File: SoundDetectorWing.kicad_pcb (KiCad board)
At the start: 2 copper layers, 50.8 x 22.9 mm, 17 parts, among them J1 feather long, J2 feather short, J3 sound detector

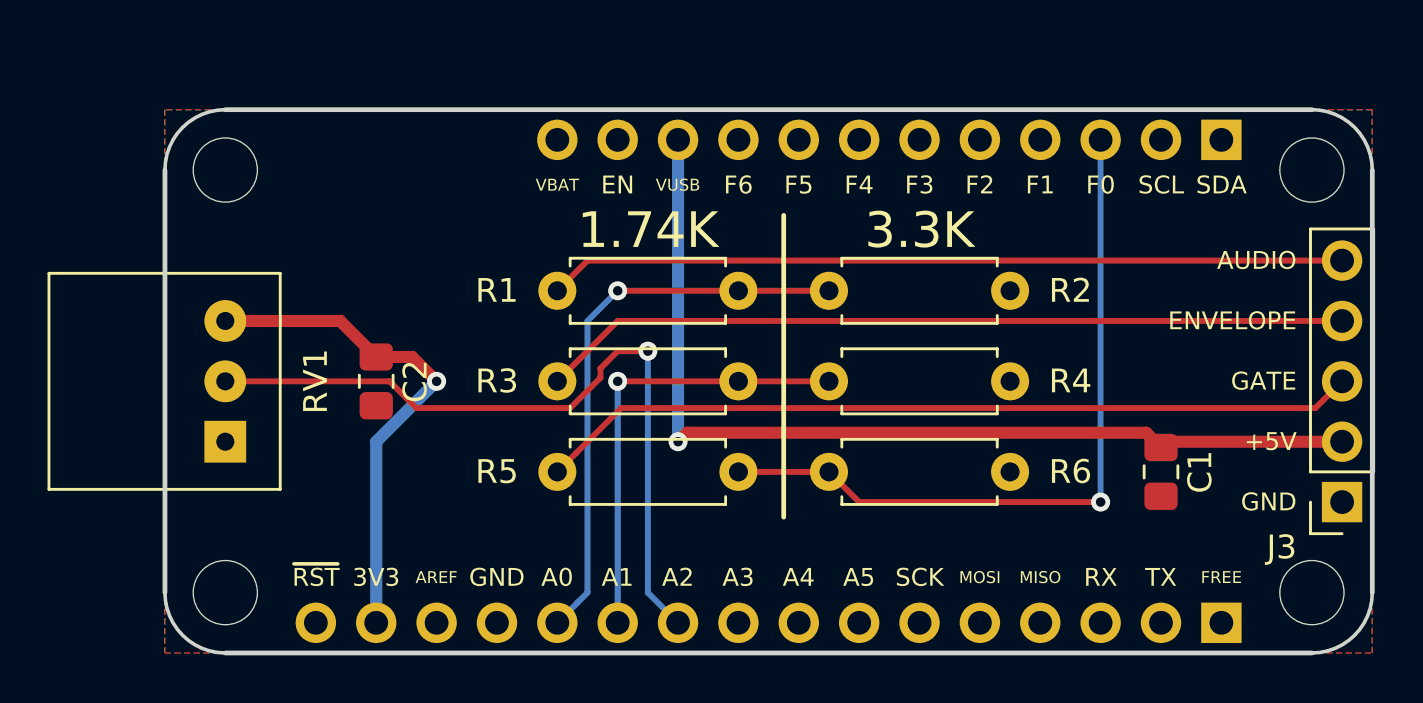
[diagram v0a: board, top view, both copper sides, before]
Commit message: Add screw holes to line up with SparkFun Sound Detector board.
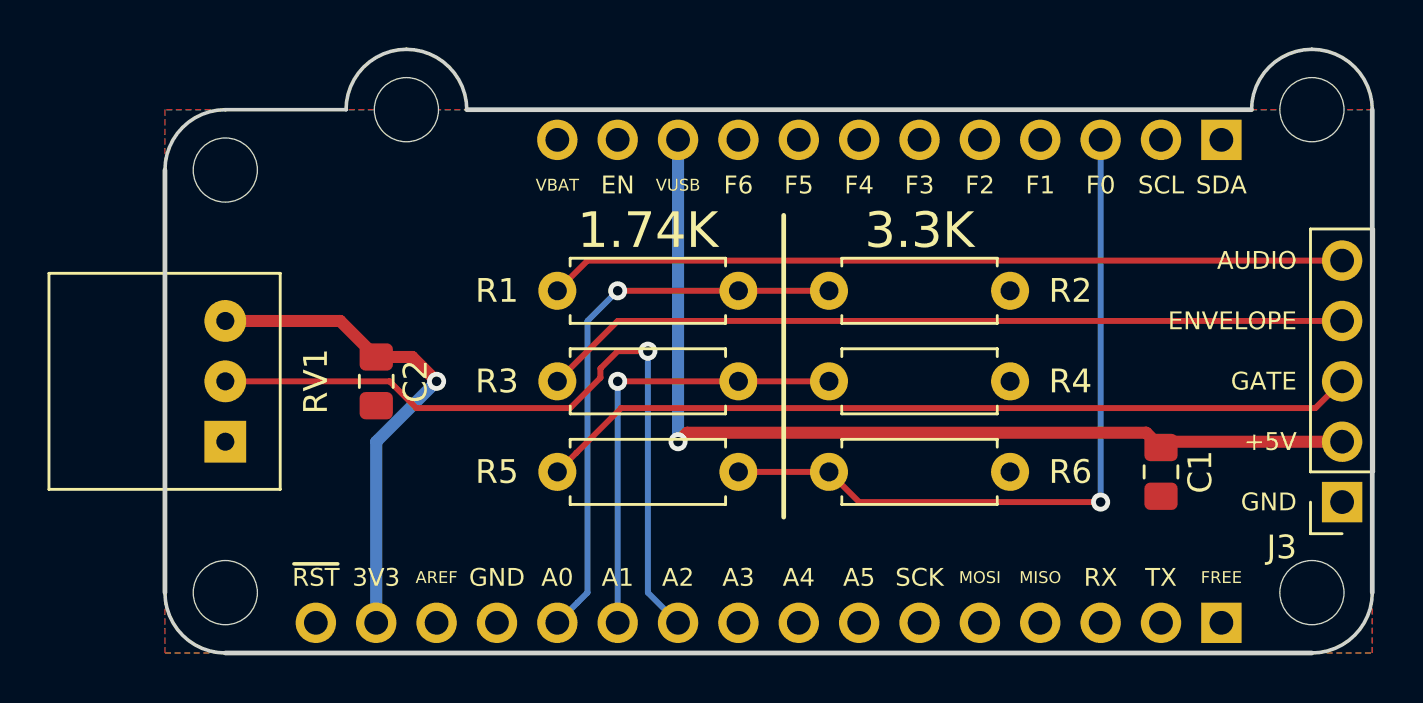
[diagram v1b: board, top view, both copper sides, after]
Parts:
- added REF**: MountingHole_2.7mm_M2.5, MountingHole:MountingHole_2.7mm_M2.5, F.Cu at (35.6, 25.4)
- moved REF** 2.54 mm to (73.7, 25.4)
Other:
- board size 50.8 x 22.9 mm -> 50.8 x 25.4 mm
- board text added: "2019-08-09"
- board text added: "Sound Detector FeatherWing 1.0.1"
- board text removed: "2019-07-24"
- board text removed: "Sound Detector FeatherWing 1.0"
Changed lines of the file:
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@@
   (general
     (thickness 1.6)
-    (drawings 49)
+    (drawings 53)
     (tracks 48)
     (zones 0)
-    (modules 17)
+    (modules 18)
     (nets 32)
   )
@@
   (title_block
     (title "Sound Detector FeatherWing")
-    (date 2019-07-24)
-    (rev 1.0)
+    (date 2019-08-09)
+    (rev 1.0.1)
     (company "Patrick Pelletier")
   )
@@
   )
   (module MountingHole:MountingHole_2.7mm_M2.5 locked (layer F.Cu)
-    (at 73.66 27.94)
+    (at 35.56 25.4)
+    (descr "Mounting Hole 2.7mm, no annular, M2.5")
+    (tags "mounting hole 2.7mm no annular m2.5")
+    (attr virtual)
+    (fp_text reference REF** (at 0 -3.7) (layer F.SilkS) hide
+      (effects (font (size 1 1) (thickness 0.15)))
+    )
+    (fp_text value MountingHole_2.7mm_M2.5 (at 0 3.7) (layer F.Fab) hide
+      (effects (font (size 1 1) (thickness 0.15)))
+    )
+    (fp_circle (center 0 0) (end 2.95 0) (layer F.CrtYd) (width 0.05))
+    (fp_circle (center 0 0) (end 2.7 0) (layer Cmts.User) (width 0.15))
+    (fp_text user %R (at 0.3 0) (layer F.Fab) hide
+      (effects (font (size 1 1) (thickness 0.15)))
+    )
+    (pad 1 np_thru_hole circle (at 0 0) (size 2.7 2.7) (drill 2.7) (layers *.Cu *.Mask))
+  )
+  (module MountingHole:MountingHole_2.7mm_M2.5 locked (layer F.Cu)
+    (at 73.66 25.4)
     (descr "Mounting Hole 2.7mm, no annular, M2.5")
     (tags "mounting hole 2.7mm no annular m2.5")
@@
       (xy 0.555814 2.531069)) (layer B.SilkS) (width 0.01))
   )
+  (gr_line (start 33.02 25.4) (end 27.94 25.4) (layer Edge.Cuts) (width 0.15))
+  (gr_arc (start 35.56 25.4) (end 35.56 22.86) (angle -90) (layer Edge.Cuts) (width 0.15))
+  (gr_arc (start 35.56 25.4) (end 38.1 25.4) (angle -90) (layer Edge.Cuts) (width 0.15))
+  (gr_arc (start 73.66 25.4) (end 73.66 22.86) (angle -90) (layer Edge.Cuts) (width 0.15))
   (gr_text https://github.com/ppelleti/SoundDetectorWing (at 51.435 34.925) (layer B.SilkS)
     (effects (font (size 0.75 0.75) (thickness 0.15)) (justify mirror))
@@
     (effects (font (size 1 1) (thickness 0.2)) (justify mirror))
   )
-  (gr_text 2019-07-24 (at 31.75 36.83 90) (layer B.SilkS)
+  (gr_text 2019-08-09 (at 31.75 36.83 90) (layer B.SilkS)
     (effects (font (size 1.5 1.5) (thickness 0.3)) (justify mirror))
   )
@@
     (effects (font (size 1.5 1.5) (thickness 0.3)) (justify mirror))
   )
-  (gr_text "Sound Detector FeatherWing 1.0" (at 53.34 30.48) (layer B.SilkS)
+  (gr_text "Sound Detector FeatherWing 1.0.1" (at 53.34 30.48) (layer B.SilkS)
     (effects (font (size 1.5 1.5) (thickness 0.3)) (justify mirror))
   )
@@
     (effects (font (size 0.75 0.75) (thickness 0.15)))
   )
-  (gr_arc (start 73.66 27.94) (end 76.2 27.94) (angle -90) (layer Edge.Cuts) (width 0.15))
+  (gr_arc (start 73.66 25.4) (end 76.2 25.4) (angle -90) (layer Edge.Cuts) (width 0.15))
   (gr_arc (start 73.66 45.72) (end 73.66 48.26) (angle -90) (layer Edge.Cuts) (width 0.15))
   (gr_arc (start 27.94 45.72) (end 25.4 45.72) (angle -90) (layer Edge.Cuts) (width 0.15))
@@
   (gr_line (start 25.4 45.72) (end 25.4 27.94) (layer Edge.Cuts) (width 0.2))
   (gr_line (start 73.66 48.26) (end 27.94 48.26) (layer Edge.Cuts) (width 0.2))
-  (gr_line (start 76.2 27.94) (end 76.2 45.72) (layer Edge.Cuts) (width 0.2))
-  (gr_line (start 27.94 25.4) (end 73.66 25.4) (layer Edge.Cuts) (width 0.2))
+  (gr_line (start 76.2 25.4) (end 76.2 45.72) (layer Edge.Cuts) (width 0.2))
+  (gr_line (start 38.1 25.4) (end 71.12 25.4) (layer Edge.Cuts) (width 0.2))
   (segment (start 43.724999 36.680003) (end 43.724999 36.285001) (width 0.25) (layer F.Cu) (net 10))
   (segment (start 27.94 36.83) (end 34.85319 36.83) (width 0.25) (layer F.Cu) (net 10))

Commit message: Label the functions of the feather pins.
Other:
- board text added: "ENV"
- board text added: "POT"
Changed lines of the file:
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@@
   (general
     (thickness 1.6)
-    (drawings 53)
+    (drawings 57)
     (tracks 48)
     (zones 0)
@@
       (xy 0.555814 2.531069)) (layer B.SilkS) (width 0.01))
   )
+  (gr_text POT (at 46.99 44.45 90) (layer F.SilkS)
+    (effects (font (size 0.75 0.75) (thickness 0.15)) (justify left))
+  )
+  (gr_text ENV (at 44.45 44.45 90) (layer F.SilkS)
+    (effects (font (size 0.75 0.75) (thickness 0.15)) (justify left))
+  )
+  (gr_text AUDIO (at 41.91 44.45 90) (layer F.SilkS)
+    (effects (font (size 0.5 0.5) (thickness 0.1)) (justify left))
+  )
+  (gr_text GATE (at 64.77 29.21 90) (layer F.SilkS)
+    (effects (font (size 0.75 0.75) (thickness 0.15)) (justify right))
+  )
   (gr_line (start 33.02 25.4) (end 27.94 25.4) (layer Edge.Cuts) (width 0.15))

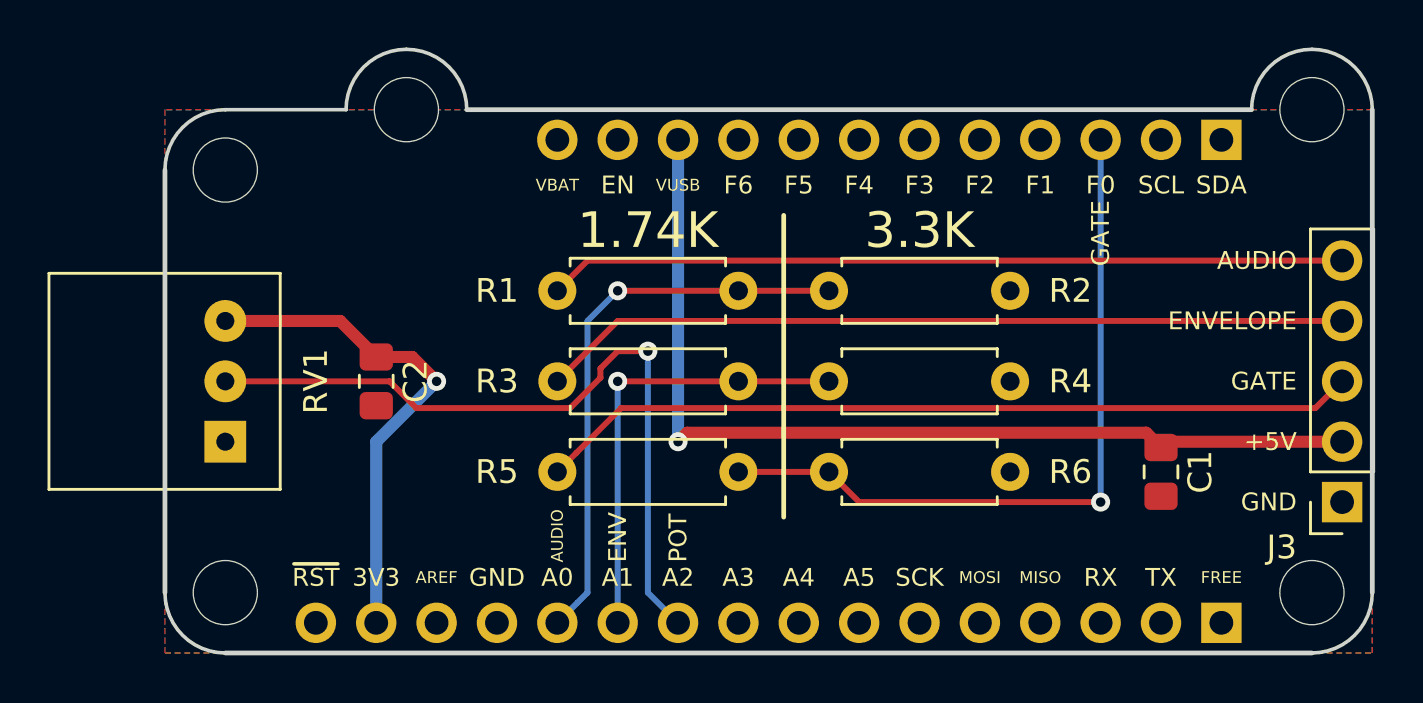
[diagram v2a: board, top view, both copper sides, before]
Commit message: Finally get SoundDetector mounting holes in correct place.
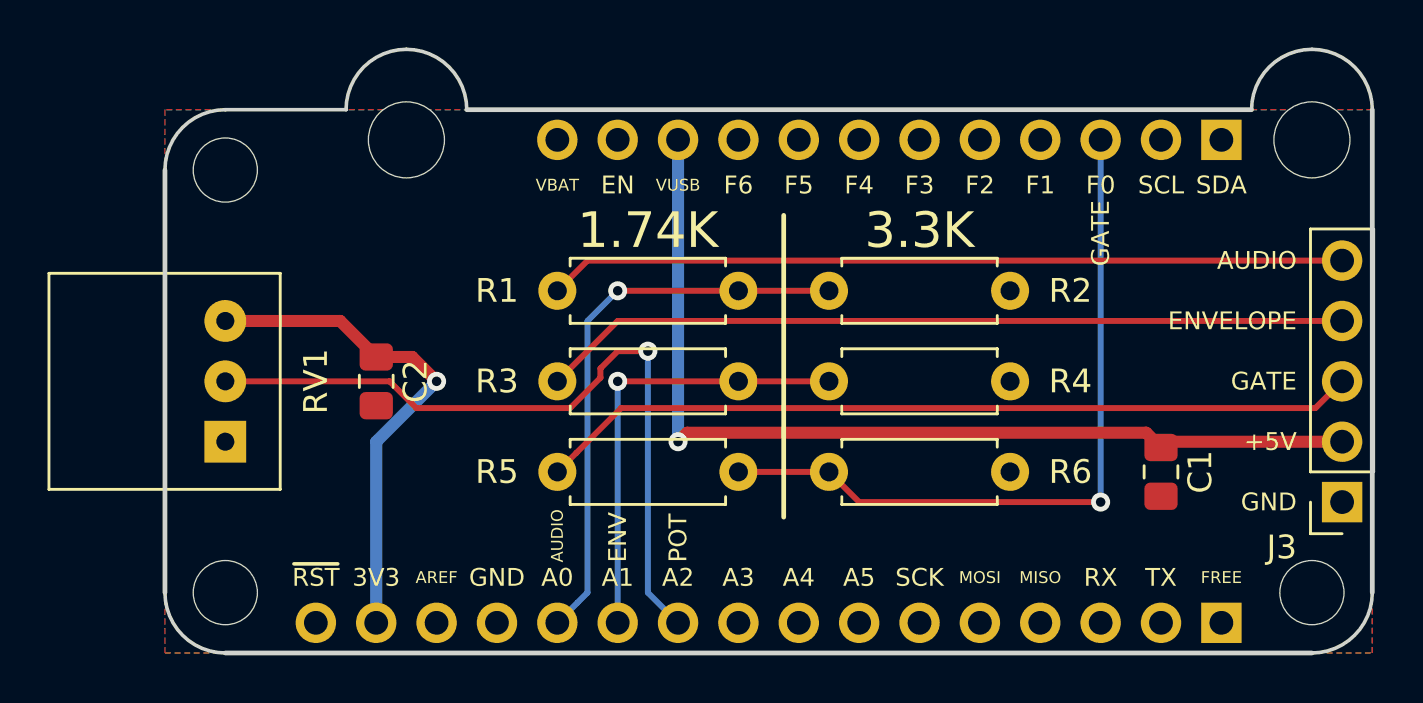
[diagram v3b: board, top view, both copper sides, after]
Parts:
- removed the REF** at (35.6, 25.4)
- removed the REF** at (73.7, 25.4)
- added REF**: MountingHole_3.2mm_M3, MountingHole:MountingHole_3.2mm_M3, F.Cu at (73.7, 26.7)
- added REF**: MountingHole_3.2mm_M3, MountingHole:MountingHole_3.2mm_M3, F.Cu at (35.6, 26.7)
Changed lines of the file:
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@@
     (add_net GND)
   )
-  (module MountingHole:MountingHole_2.7mm_M2.5 locked (layer F.Cu)
-    (at 35.56 25.4)
-    (descr "Mounting Hole 2.7mm, no annular, M2.5")
-    (tags "mounting hole 2.7mm no annular m2.5")
+  (module MountingHole:MountingHole_3.2mm_M3 (layer F.Cu)
+    (at 73.66 26.67)
+    (descr "Mounting Hole 3.2mm, no annular, M3")
+    (tags "mounting hole 3.2mm no annular m3")
     (attr virtual)
-    (fp_text reference REF** (at 0 -3.7) (layer F.SilkS) hide
-      (effects (font (size 1 1) (thickness 0.15)))
-    )
-    (fp_text value MountingHole_2.7mm_M2.5 (at 0 3.7) (layer F.Fab) hide
-      (effects (font (size 1 1) (thickness 0.15)))
-    )
-    (fp_circle (center 0 0) (end 2.95 0) (layer F.CrtYd) (width 0.05))
-    (fp_circle (center 0 0) (end 2.7 0) (layer Cmts.User) (width 0.15))
+    (fp_text reference REF** (at 0 -4.2) (layer F.SilkS) hide
+      (effects (font (size 1 1) (thickness 0.15)))
+    )
+    (fp_text value MountingHole_3.2mm_M3 (at 0 4.2) (layer F.Fab) hide
+      (effects (font (size 1 1) (thickness 0.15)))
+    )
     (fp_text user %R (at 0.3 0) (layer F.Fab) hide
       (effects (font (size 1 1) (thickness 0.15)))
     )
-    (pad 1 np_thru_hole circle (at 0 0) (size 2.7 2.7) (drill 2.7) (layers *.Cu *.Mask))
-  )
-  (module MountingHole:MountingHole_2.7mm_M2.5 locked (layer F.Cu)
-    (at 73.66 25.4)
-    (descr "Mounting Hole 2.7mm, no annular, M2.5")
-    (tags "mounting hole 2.7mm no annular m2.5")
-    (attr virtual)
-    (fp_text reference REF** (at 0 -3.7) (layer F.SilkS) hide
-      (effects (font (size 1 1) (thickness 0.15)))
-    )
-    (fp_text value MountingHole_2.7mm_M2.5 (at 0 3.7) (layer F.Fab) hide
-      (effects (font (size 1 1) (thickness 0.15)))
-    )
-    (fp_text user %R (at 0.3 0) (layer F.Fab) hide
-      (effects (font (size 1 1) (thickness 0.15)))
-    )
-    (fp_circle (center 0 0) (end 2.7 0) (layer Cmts.User) (width 0.15))
-    (fp_circle (center 0 0) (end 2.95 0) (layer F.CrtYd) (width 0.05))
-    (pad 1 np_thru_hole circle (at 0 0) (size 2.7 2.7) (drill 2.7) (layers *.Cu *.Mask))
+    (fp_circle (center 0 0) (end 3.2 0) (layer Cmts.User) (width 0.15))
+    (fp_circle (center 0 0) (end 3.45 0) (layer F.CrtYd) (width 0.05))
+    (pad 1 np_thru_hole circle (at 0 0) (size 3.2 3.2) (drill 3.2) (layers *.Cu *.Mask))
   )
   (module MountingHole:MountingHole_2.7mm_M2.5 locked (layer F.Cu)
@@
       (xy 0.555814 2.531069)) (layer B.SilkS) (width 0.01))
   )
+  (module MountingHole:MountingHole_3.2mm_M3 (layer F.Cu)
+    (at 35.56 26.67)
+    (descr "Mounting Hole 3.2mm, no annular, M3")
+    (tags "mounting hole 3.2mm no annular m3")
+    (attr virtual)
+    (fp_text reference REF** (at 0 -4.2) (layer F.SilkS) hide
+      (effects (font (size 1 1) (thickness 0.15)))
+    )
+    (fp_text value MountingHole_3.2mm_M3 (at 0 4.2) (layer F.Fab) hide
+      (effects (font (size 1 1) (thickness 0.15)))
+    )
+    (fp_circle (center 0 0) (end 3.45 0) (layer F.CrtYd) (width 0.05))
+    (fp_circle (center 0 0) (end 3.2 0) (layer Cmts.User) (width 0.15))
+    (fp_text user %R (at 0.3 0) (layer F.Fab) hide
+      (effects (font (size 1 1) (thickness 0.15)))
+    )
+    (pad 1 np_thru_hole circle (at 0 0) (size 3.2 3.2) (drill 3.2) (layers *.Cu *.Mask))
+  )
   (gr_text POT (at 46.99 44.45 90) (layer F.SilkS)

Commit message: Adjust board outline.
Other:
- board size 50.8 x 25.4 mm -> 50.8 x 24.1 mm
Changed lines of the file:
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@@
   (general
     (thickness 1.6)
-    (drawings 57)
+    (drawings 59)
     (tracks 48)
     (zones 0)
@@
     (add_net GND)
   )
-  (module MountingHole:MountingHole_3.2mm_M3 (layer F.Cu)
+  (module MountingHole:MountingHole_3.2mm_M3 locked (layer F.Cu)
     (at 73.66 26.67)
     (descr "Mounting Hole 3.2mm, no annular, M3")
@@
       (xy 0.555814 2.531069)) (layer B.SilkS) (width 0.01))
   )
-  (module MountingHole:MountingHole_3.2mm_M3 (layer F.Cu)
+  (module MountingHole:MountingHole_3.2mm_M3 locked (layer F.Cu)
     (at 35.56 26.67)
     (descr "Mounting Hole 3.2mm, no annular, M3")
@@
     (pad 1 np_thru_hole circle (at 0 0) (size 3.2 3.2) (drill 3.2) (layers *.Cu *.Mask))
   )
+  (gr_line (start 74.93 24.13) (end 72.39 24.13) (layer Edge.Cuts) (width 0.15))
+  (gr_arc (start 72.39 25.4) (end 72.39 24.13) (angle -90) (layer Edge.Cuts) (width 0.15))
+  (gr_arc (start 74.93 25.4) (end 76.2 25.4) (angle -90) (layer Edge.Cuts) (width 0.15))
+  (gr_line (start 34.29 24.13) (end 36.83 24.13) (layer Edge.Cuts) (width 0.15))
+  (gr_arc (start 34.29 25.4) (end 34.29 24.13) (angle -90) (layer Edge.Cuts) (width 0.2))
+  (gr_arc (start 36.83 25.4) (end 38.1 25.4) (angle -90) (layer Edge.Cuts) (width 0.2))
   (gr_text POT (at 46.99 44.45 90) (layer F.SilkS)
     (effects (font (size 0.75 0.75) (thickness 0.15)) (justify left))
@@
   )
   (gr_line (start 33.02 25.4) (end 27.94 25.4) (layer Edge.Cuts) (width 0.15))
-  (gr_arc (start 35.56 25.4) (end 35.56 22.86) (angle -90) (layer Edge.Cuts) (width 0.15))
-  (gr_arc (start 35.56 25.4) (end 38.1 25.4) (angle -90) (layer Edge.Cuts) (width 0.15))
-  (gr_arc (start 73.66 25.4) (end 73.66 22.86) (angle -90) (layer Edge.Cuts) (width 0.15))
   (gr_text https://github.com/ppelleti/SoundDetectorWing (at 51.435 34.925) (layer B.SilkS)
     (effects (font (size 0.75 0.75) (thickness 0.15)) (justify mirror))
@@
     (effects (font (size 0.75 0.75) (thickness 0.15)))
   )
-  (gr_arc (start 73.66 25.4) (end 76.2 25.4) (angle -90) (layer Edge.Cuts) (width 0.15))
   (gr_arc (start 73.66 45.72) (end 73.66 48.26) (angle -90) (layer Edge.Cuts) (width 0.15))
   (gr_arc (start 27.94 45.72) (end 25.4 45.72) (angle -90) (layer Edge.Cuts) (width 0.15))

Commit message: Update version number.
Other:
- board text added: "2019-08-22"
- board text added: "Sound Detector FeatherWing 1.0.2"
- board text removed: "2019-08-09"
- board text removed: "Sound Detector FeatherWing 1.0.1"
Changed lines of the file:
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@@
   (title_block
     (title "Sound Detector FeatherWing")
-    (date 2019-08-09)
-    (rev 1.0.1)
+    (date 2019-08-22)
+    (rev 1.0.2)
     (company "Patrick Pelletier")
   )
@@
     (effects (font (size 1 1) (thickness 0.2)) (justify mirror))
   )
-  (gr_text 2019-08-09 (at 31.75 36.83 90) (layer B.SilkS)
+  (gr_text 2019-08-22 (at 31.75 36.83 90) (layer B.SilkS)
     (effects (font (size 1.5 1.5) (thickness 0.3)) (justify mirror))
   )
@@
     (effects (font (size 1.5 1.5) (thickness 0.3)) (justify mirror))
   )
-  (gr_text "Sound Detector FeatherWing 1.0.1" (at 53.34 30.48) (layer B.SilkS)
+  (gr_text "Sound Detector FeatherWing 1.0.2" (at 53.34 30.48) (layer B.SilkS)
     (effects (font (size 1.5 1.5) (thickness 0.3)) (justify mirror))
   )
